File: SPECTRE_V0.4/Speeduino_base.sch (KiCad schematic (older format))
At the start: 178 parts, among them J1 Conn_01x04_Male, Q1 2N7002, Q10 BSP78, Q11 BSP78, Q12 BSP78, Q13 BSP78, Q14 BSP78, Q15 BSP78, Q16 BSP78, Q17 BSP78, Q18 BSP78, Q2 CJ2302, Q3 CJ2302, Q4 CJ2302, Q5 BSP78, Q6 BSP78, Q7 CJ2302, Q8 CJ2302, Q9 CJ2302, U1 MAX9926UAEE+, U2 molex_48pin, U3 LM78M05_TO220

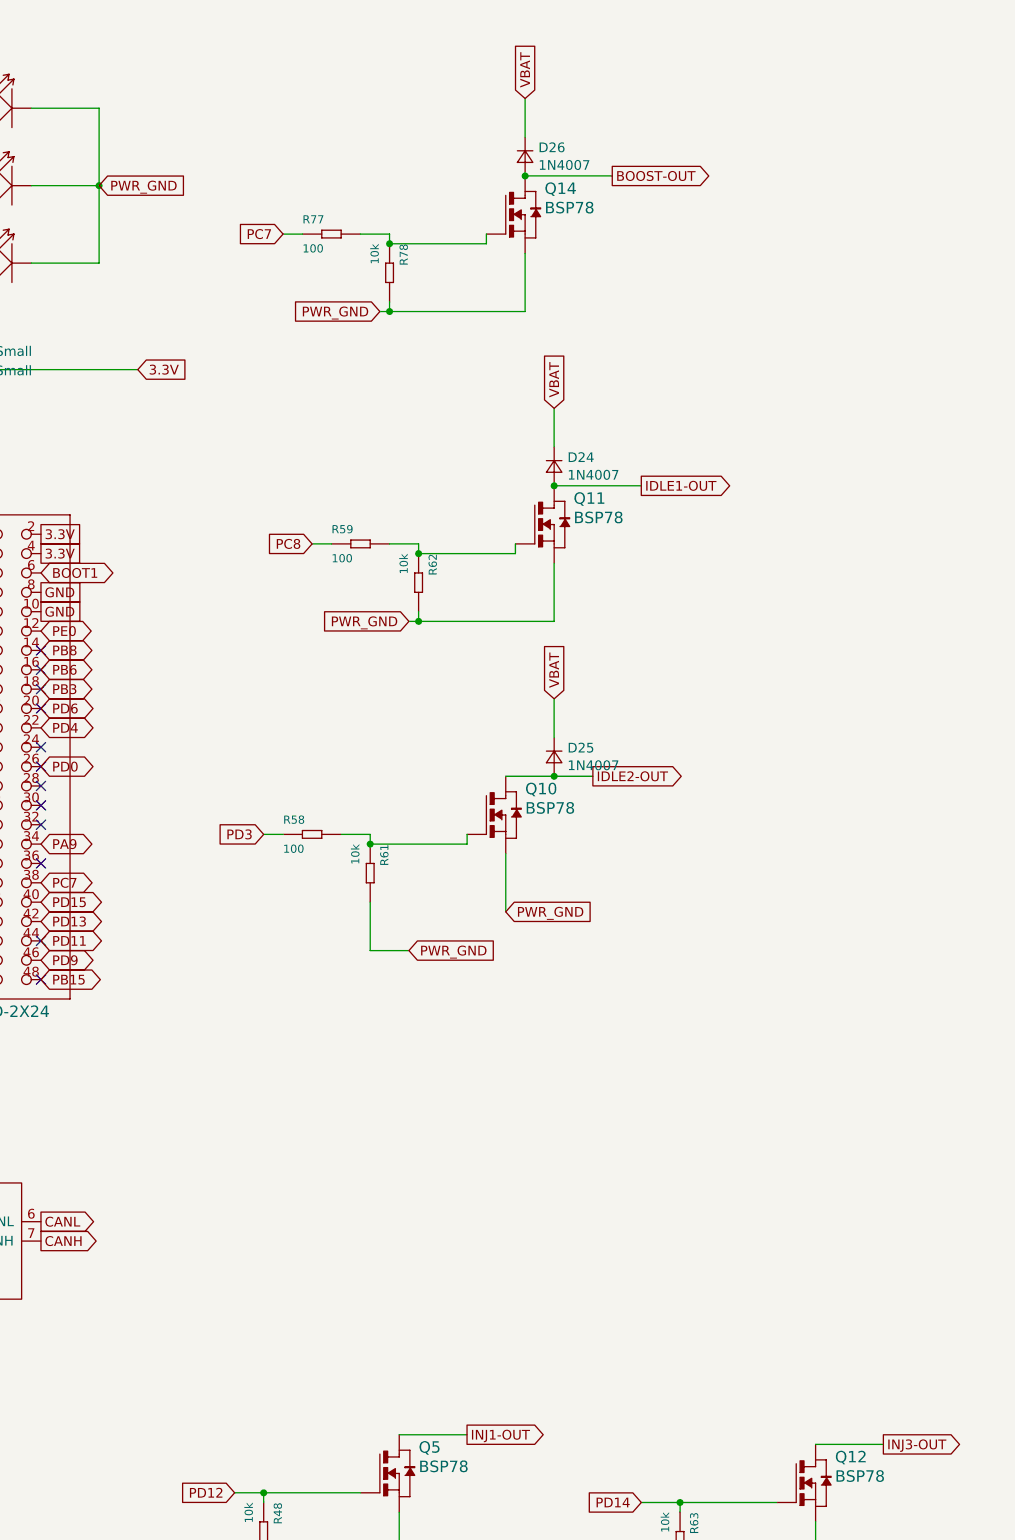
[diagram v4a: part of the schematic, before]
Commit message: rs232 header NRF
Added rs232 driver and Added NRF header to use SPI .
TODO:
- finish rs232 to 48 pin connector
- route BME280
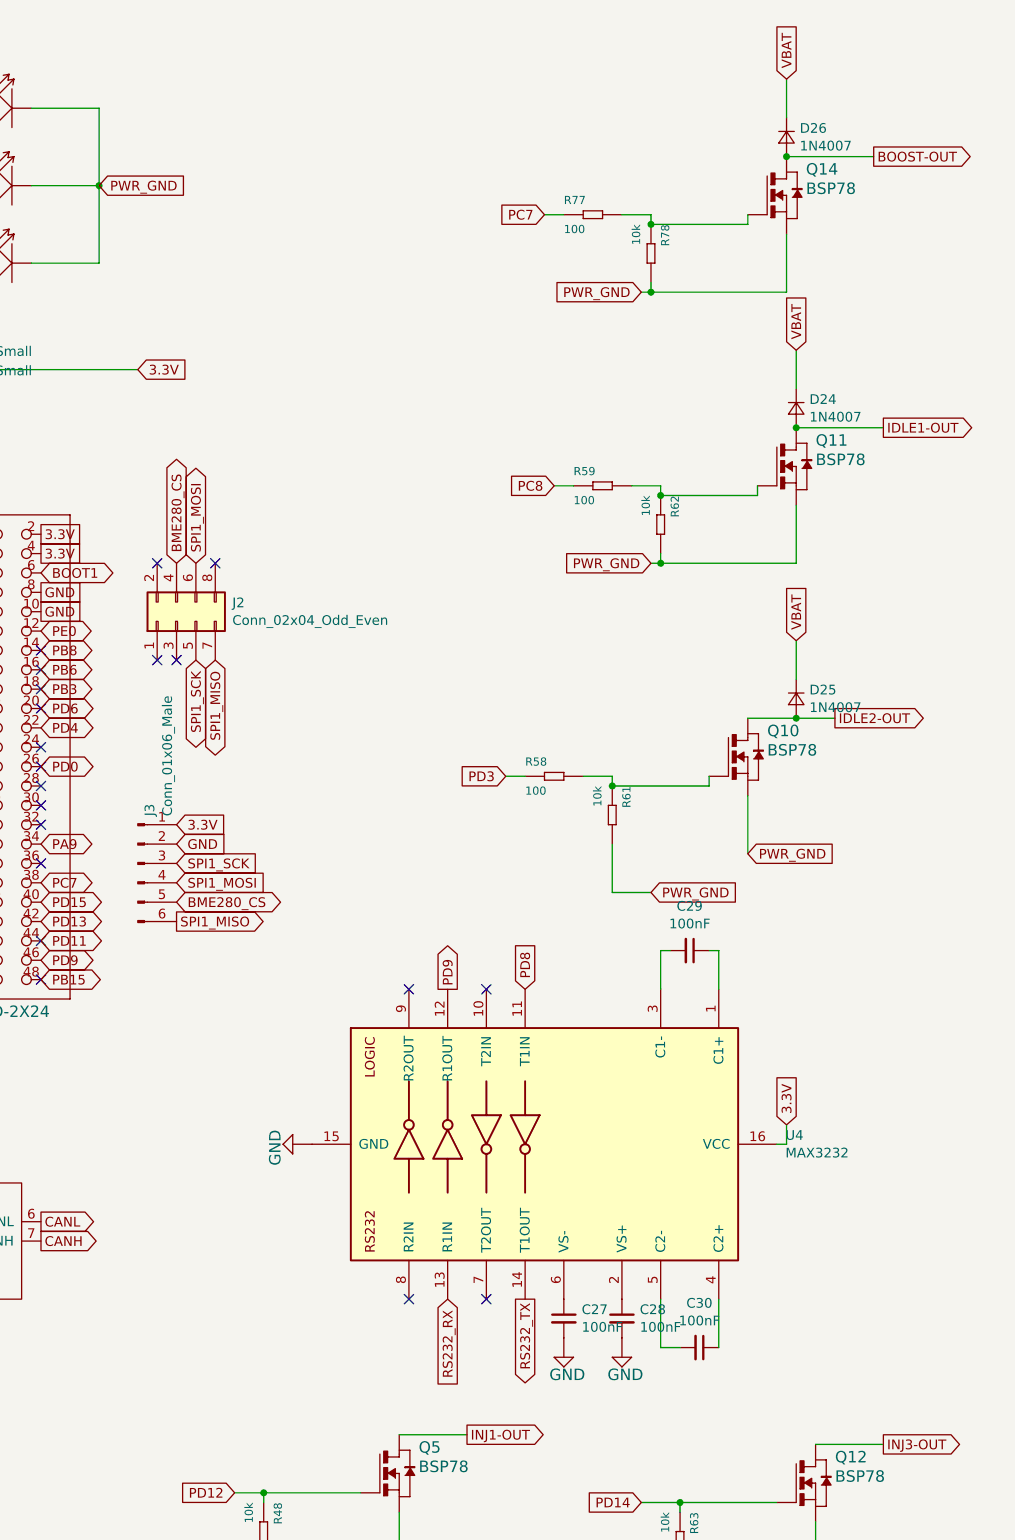
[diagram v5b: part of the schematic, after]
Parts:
- added C27, C28, C29, C30: 100nF, Capacitor_SMD:C_0603_1608Metric, symbol Device:C_Small
- added J2: Conn_02x04_Odd_Even, Connector_PinHeader_2.54mm:PinHeader_2x04_P2.54mm_Vertical, symbol Connector_Generic:Conn_02x04_Odd_Even
- added J3: Conn_01x06_Male, Connector_PinHeader_2.54mm:PinHeader_1x06_P2.54mm_Vertical, symbol Connector:Conn_01x06_Male
- added U4: MAX3232, Package_SO:SOIC-16_4.55x10.3mm_P1.27mm, symbol Interface_UART:MAX3232
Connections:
- net labels added: BME280_CS, RS232_RX, RS232_TX, SPI1_MISO, SPI1_MOSI, SPI1_SCK
- wire segments 493 -> 502
- no-connect marks 49 -> 57
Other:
- moved on the sheet: D24, D25, D26, Q10, Q11, Q14, R58, R59, R61, R62, R77, R78

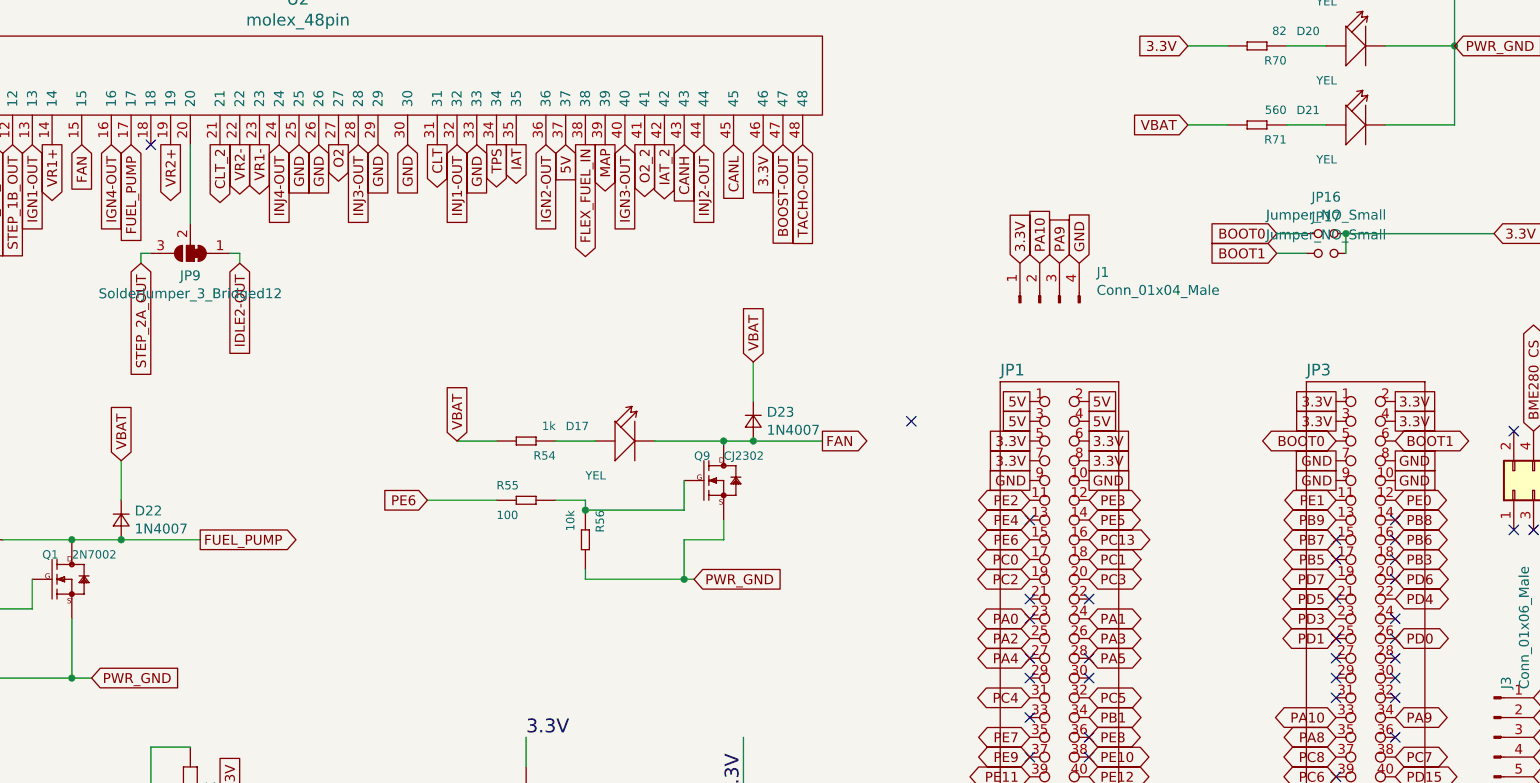
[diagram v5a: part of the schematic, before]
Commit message: rs232 + BME280 finished
Added rs232 to connector
Finished BME280 connection and routing
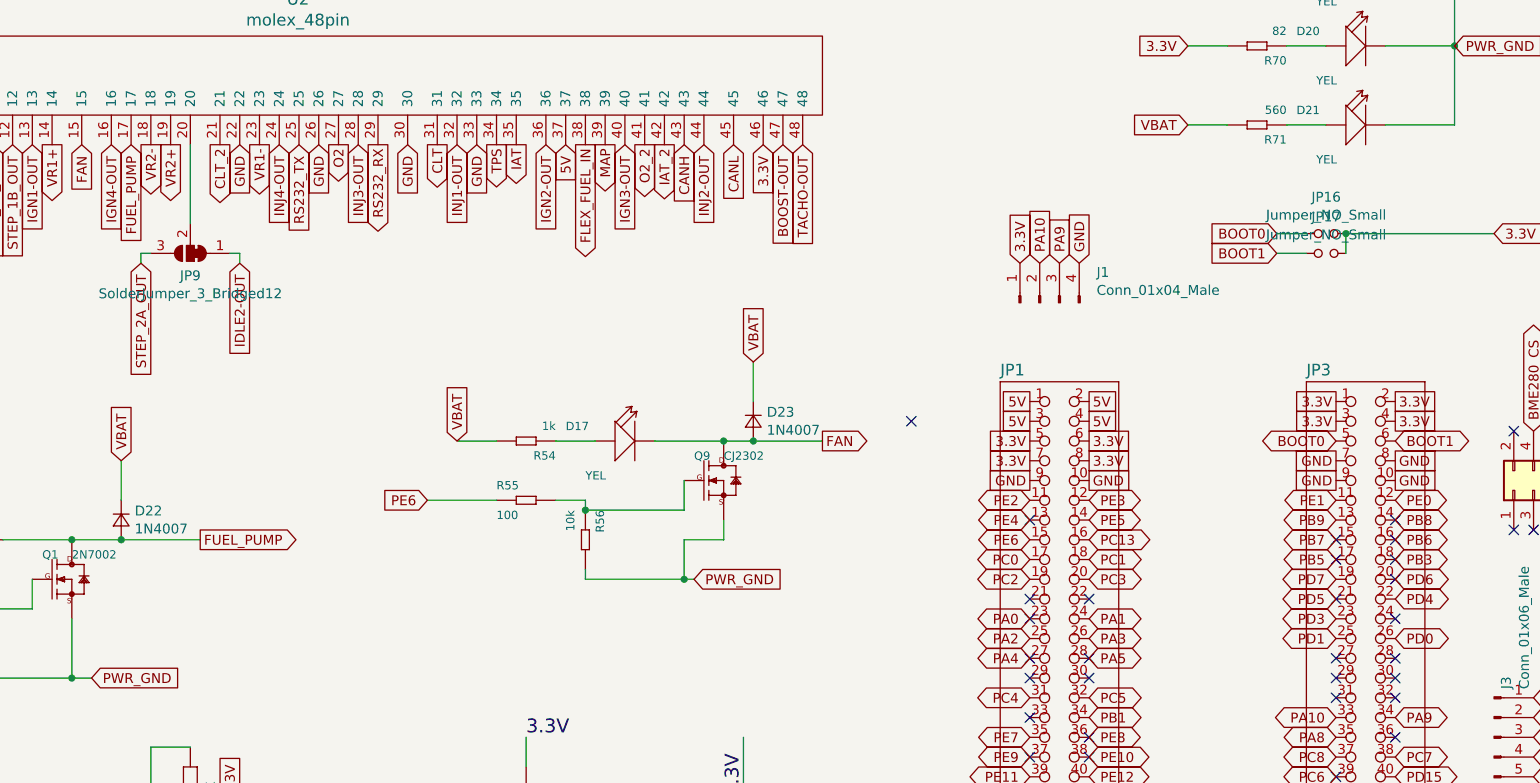
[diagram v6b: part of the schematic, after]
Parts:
- J2: footprint Connector_PinHeader_2.54mm:PinHeader_2x04_P2.54mm_Vertical -> Speeduino_base:PinHeader_2x04_P2.54mm_Vertical
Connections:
- no-connect marks 57 -> 54
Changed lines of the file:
@@
 Text GLabel 8050 1400 3    50   Output ~ 0
 MAP
-Text GLabel 7050 1400 3    50   Input ~ 0
-GND
 Text GLabel 6600 1400 3    50   Input ~ 0
 GND
@@
 Text GLabel 5850 1400 3    50   Output ~ 0
 VR2+
-Text GLabel 6200 1400 3    50   Output ~ 0
+Text GLabel 5750 1400 3    50   Output ~ 0
 VR2-
 Text GLabel 6300 1400 3    50   Output ~ 0
@@
 Wire Wire Line
 	750  10300 750  10400
-Text GLabel 6500 1400 3    50   Input ~ 0
+Text GLabel 6200 1400 3    50   Input ~ 0
 GND
-Text GLabel 6900 1400 3    50   Input ~ 0
+Text GLabel 7050 1400 3    50   Input ~ 0
 GND
 Text GLabel 7400 1400 3    50   Input ~ 0
@@
 	1    0    0    -1
 $EndComp
-NoConn ~ 5750 1400
 NoConn ~ 10200 4000
 NoConn ~ 9600 2800
@@
 NoConn ~ 10200 4500
 NoConn ~ 10500 4400
-NoConn ~ 12050 3900
-NoConn ~ 11750 3900
 NoConn ~ 12050 3300
 NoConn ~ 11750 3400
@@
 Text GLabel 12050 6350 2    50   Output ~ 0
 CANH
-Connection ~ 4200 1400
-$Comp
-L molex_48pin:molex_48pin U2
-U 1 1 5E17AB54
-P 6900 1950
-F 0 "U2" V 8187 2355 60  0000 C CNN
-F 1 "molex_48pin" V 8081 2355 60  0000 C CNN
-F 2 "rusefi_lib:Molex_48" H 6900 1950 60  0001 C CNN
-F 3 "" H 6900 1950 60  0001 C CNN
-	1    6900 1950
-	0    -1   -1   0
-$EndComp
 Text GLabel 8450 1400 3    50   Input ~ 0
 CANH
@@
 F 0 "J2" V 12846 2862 50  0000 R CNN
 F 1 "Conn_02x04_Odd_Even" V 12755 2862 50  0000 R CNN
-F 2 "Connector_PinHeader_2.54mm:PinHeader_2x04_P2.54mm_Vertical" H 12750 3150 50  0001 C CNN
+F 2 "Speeduino_base:PinHeader_2x04_P2.54mm_Vertical" H 12750 3150 50  0001 C CNN
 F 3 "~" H 12750 3150 50  0001 C CNN
 	1    12750 3150
@@
 Text GLabel 12750 4700 2    50   Output ~ 0
 SPI1_MISO
+Text GLabel 6500 1400 3    50   Input ~ 0
+RS232_TX
+Connection ~ 4200 1400
+$Comp
+L molex_48pin:molex_48pin U2
+U 1 1 5E17AB54
+P 6900 1950
+F 0 "U2" V 8187 2355 60  0000 C CNN
+F 1 "molex_48pin" V 8081 2355 60  0000 C CNN
+F 2 "rusefi_lib:Molex_48" H 6900 1950 60  0001 C CNN
+F 3 "" H 6900 1950 60  0001 C CNN
+	1    6900 1950
+	0    -1   -1   0
+$EndComp
+Text GLabel 6900 1400 3    50   Output ~ 0
+RS232_RX
 $EndSCHEMATC
